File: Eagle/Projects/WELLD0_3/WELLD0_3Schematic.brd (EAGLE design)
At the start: 160 x 100 mm, 17 parts, among them J2 Battery, U1 EFM8BB10F8G-µCBRZ, U2 CJT1117-3.3-SOT223, X1 ProgramPins

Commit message: Circuit done - i guess 24/10-18
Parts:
- removed R1: 10K, audio amplifier example:R0603
- removed S1: Switch, SparkFun-Switches:TACTILE_SWITCH_SMD_6.2MM_TALL
- removed T1: (no value), DC_LOAD_AU:SOT23-BEC
- removed U1: EFM8BB10F8G-µCBRZ, adg451_adg452_adg453:SO16
- added ALT_USER_SW1, ALT_USER_SW2, ALT_USER_SW3, ALT_USER_SW4, LED+, LED-: (no value), SparkFun-Connectors:1X01
- added BOOTLOADER, RST_SW, USER_SW, USER_SW_ALT: Switch, SparkFun-Switches:TACTILE_SWITCH_SMD_6.2MM_TALL
- added C1, C2: 100nF, rcl:C0603
- added IC1: STM32F030F4P6TR, SamacSys_Parts:SOP65P640X120-20N
- added R2, R4: 10k, audio amplifier example:R0603
- added R3, R6: 10K, audio amplifier example:R0603
- added R5: R>12.5k, audio amplifier example:R0603
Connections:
- removed net C2D: U1.7, X1.3
- removed net P0.6: U1.13
- removed net P0.7: U1.12
- removed net RSTB/C2CI: U1.6, X1.2
- removed net SWSIGN: R1.1, S1.A2, U1.14
- removed net VDD: R1.2, U1.5, U2.2, U2.TER
- new net +3.3V: BOOTLOADER.A2, IC1.16, IC1.5, R3.2, R6.2, U2.2, U2.TER
- new net ADC_BATTERY: IC1.6, R4.2, R5.1
- new net N$4: ALT_USER_SW3.1, USER_SW_ALT.A2
- new net N$5: ALT_USER_SW4.1, USER_SW_ALT.B2
- new net N$6: IC1.1, R2.1
- new net NRST: C1.1, IC1.4, R6.1, RST_SW.B2
- new net SWSIGN1: ALT_USER_SW1.1, C2.1, IC1.13, R3.1, USER_SW.A2
- new net UART_RX: IC1.18, X1.2
- new net UART_TX: IC1.17, X1.3
- net +7.4V: now also R5.2
- net DIM: now also IC1.12; no longer U1.10
- net FB: now also LED-.1
- net GND: now also ALT_USER_SW2.1, BOOTLOADER.B2, C1.2, C2.2, IC1.15, R2.2, R4.1, RST_SW.A2, USER_SW.B2; no longer S1.B2, U1.4
- net INH: now also IC1.11
- net N$1: now also LED+.1

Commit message: Ready for final thoughts
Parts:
- removed X1: ProgramPins, con-molex:70543-03
- added PROGRAMPINS: (no value), con-lstb:MA04-1
- moved USER_SW_ALT 241.5 mm to (49.5, 40.6), turned to 270 degrees
- moved ALT_USER_SW4 232.3 mm to (55.9, 36.8)
- moved ALT_USER_SW3 223.6 mm to (43.2, 36.8)
- moved ALT_USER_SW2 211.9 mm to (61.0, 21.6)
- moved ALT_USER_SW1 202.8 mm to (61.0, 17.8)
- moved LED- 198.3 mm to (39.4, 27.9)
- moved LED+ 191.7 mm to (24.1, 27.9)
- moved R2 185.2 mm to (54.6, 16.5), turned to 90 degrees
- moved C2 179.5 mm to (59.7, 2.54)
- moved C1 176.9 mm to (45.7, 17.8)
- moved RST_SW 172.6 mm to (43.2, 22.9), turned to 180 degrees
- moved R6 161.4 mm to (41.9, 17.8)
- moved BOOTLOADER 157.4 mm to (53.3, 22.9), turned to 180 degrees
- moved R5 138.3 mm to (12.7, 25.4), turned to 90 degrees
- moved R4 133.3 mm to (16.5, 25.4), turned to 270 degrees
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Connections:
- net +7.4V: now also PROGRAMPINS.4
- net GND: now also PROGRAMPINS.3; no longer X1.1
- net SWSIGN1: now also IC1.8; no longer IC1.13
- net UART_RX: now also PROGRAMPINS.1; no longer X1.2
- net UART_TX: now also PROGRAMPINS.2; no longer X1.3
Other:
- board size 160 x 100 mm -> 63.5 x 47 mm

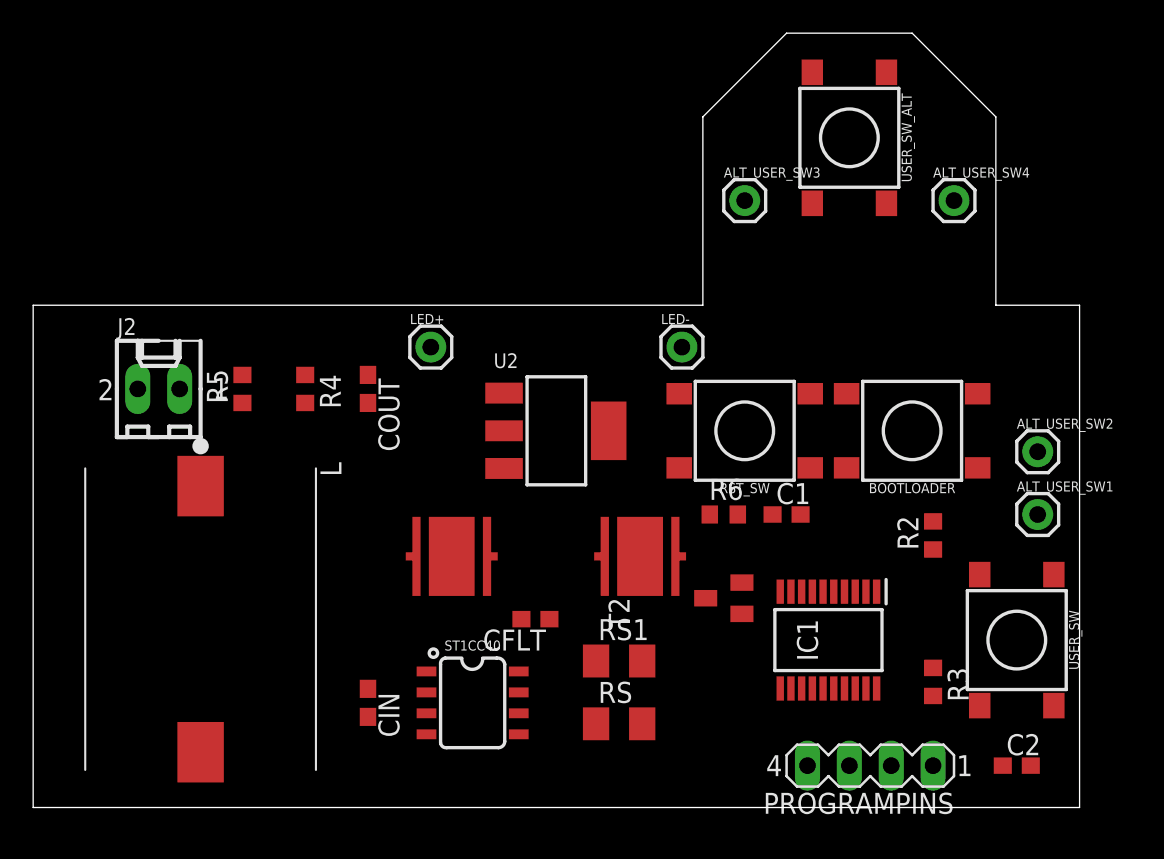
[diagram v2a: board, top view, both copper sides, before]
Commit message: Final form - missing heatsink
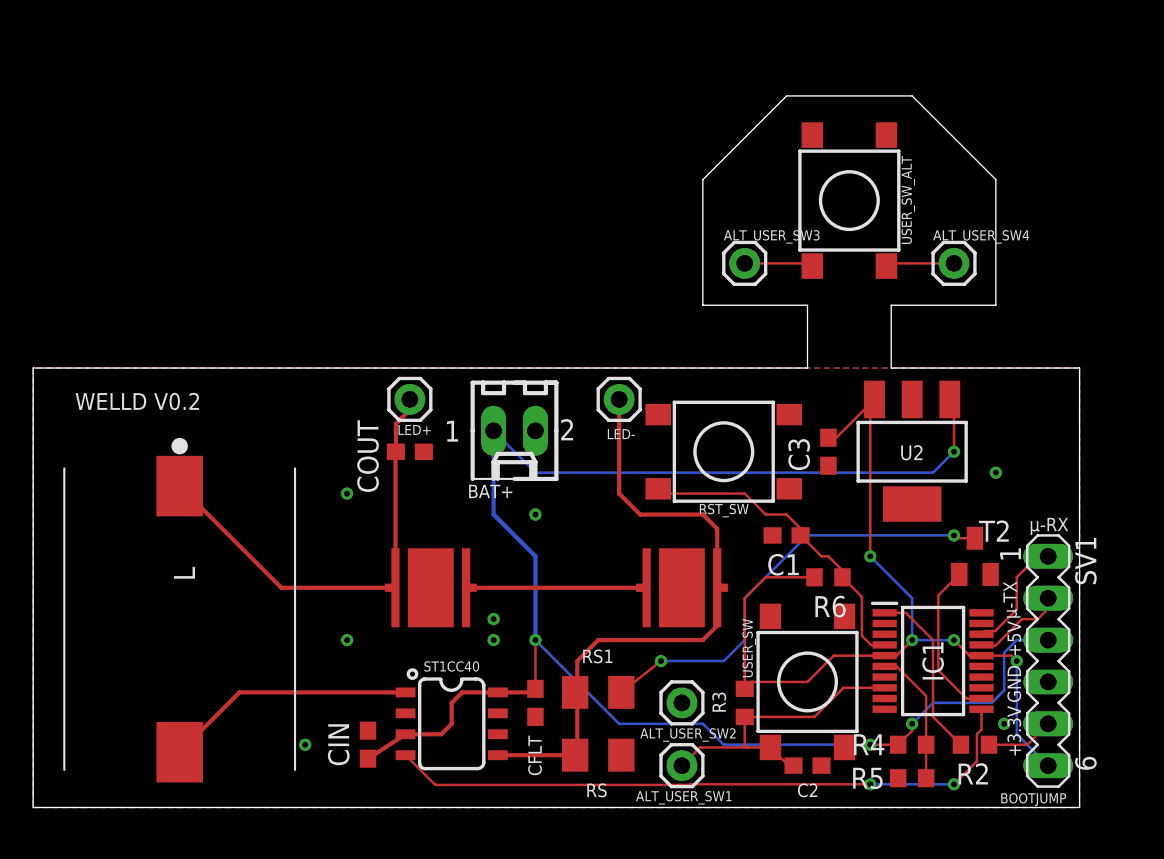
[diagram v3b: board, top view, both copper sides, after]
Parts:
- removed BOOTLOADER: Switch, SparkFun-Switches:TACTILE_SWITCH_SMD_6.2MM_TALL
- removed J2: Battery, con-molex:6410-02
- removed PROGRAMPINS: (no value), con-lstb:MA04-1
- added BAT+: BAT-, con-molex:6410-02
- added C3: 2.2µF, rcl:C0603
- added SV1: (no value), con-lstb:MA06-1
- moved R5 46.0 mm to (53.3, 3.81), turned to 180 degrees
- moved R4 43.8 mm to (53.3, 1.78), turned to 0 degrees
- moved ALT_USER_SW1 26.4 mm to (39.4, 2.54)
- moved ALT_USER_SW2 26.4 mm to (39.4, 6.35)
- moved U2 21.6 mm to (53.3, 21.6), turned to 180 degrees
- moved T2 15.5 mm to (57.1, 15.2), turned to 0 degrees
- moved R2 13.0 mm to (57.1, 3.81), turned to 0 degrees
- moved USER_SW 13.0 mm to (47.0, 7.62)
- moved C2 12.7 mm to (47.0, 2.54)
- moved R3 11.5 mm to (43.2, 6.35), turned to 90 degrees
- moved R6 7.41 mm to (48.3, 14.0), turned to 180 degrees
- moved IC1 6.48 mm to (54.6, 8.89), turned to 0 degrees
- moved CFLT 5.08 mm to (30.5, 6.35), turned to 90 degrees
- moved LED- 4.96 mm to (35.6, 24.8)
- moved COUT 4.58 mm to (22.9, 21.6), turned to 180 degrees
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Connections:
- new net BOOTJUMP: R2.2, SV1.5
- net +3.3V: now also C3.1, SV1.6, U2.3; no longer BOOTLOADER.A2, U2.2, U2.TER
- net +7.4V: now also BAT+.1, SV1.3, U2.1; no longer J2.1, PROGRAMPINS.4, U2.3
- net GND: now also BAT+.2, C3.2, SV1.4, U2.2, U2.TER; no longer BOOTLOADER.B2, J2.2, PROGRAMPINS.3, R2.2, U2.1
- net UART_RX: now also SV1.1; no longer PROGRAMPINS.1
- net UART_TX: now also SV1.2; no longer PROGRAMPINS.2
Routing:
- net +7.4V: track 0.00 -> 99.2 mm, vias 0 -> 4
- net +3.3V: track 0.00 -> 55.2 mm, vias 0 -> 4
- net FB: track 0.00 -> 39.4 mm
- net INH: track 0.00 -> 39.3 mm, vias 0 -> 2
- net N$3: track 0.00 -> 26.8 mm, vias 0 -> 2
- net N$1: track 0.00 -> 26.4 mm
- net NRST: track 0.00 -> 19.5 mm
- net SWSIGN1: track 0.00 -> 18.8 mm
- net SW: track 0.00 -> 15.2 mm
- net N$2: track 0.00 -> 11.0 mm
- net N$6: track 0.00 -> 10.7 mm
- net DIM: track 0.00 -> 9.68 mm
- net ADC_BATTERY: track 0.00 -> 7.63 mm
- net UART_RX: track 0.00 -> 7.15 mm
- net UART_TX: track 0.00 -> 5.64 mm
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- added copper zone on layer 1, net GND
- added copper zone on layer 16, net GND
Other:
- board size 63.5 x 47 mm -> 63.5 x 43.2 mm
- board text added: "+3.3V"
- board text added: "+5V"
- board text added: "BOOTJUMP"
- board text added: "GND"
- board text added: "WELLD V0.2"
- board text added: "µ-RX"
- board text added: "µ-TX"

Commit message: Ordered PCB
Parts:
- removed LED1, LED3: CREE-XLAMP-XM-L2, led:CREE-XLAMP-XM-L
- added LED2, LED4: CREE-XLAMP-XM-L, led1:CREE-XLAMP-XM-L
- moved U2 0.25 mm to (53.3, 21.3)
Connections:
- net FB: now also LED2.C, LED2.C@1; no longer LED3.C, LED3.C@1
- net GND: now also LED2.EXP, LED4.EXP
- net N$1: now also LED4.A, LED4.A@1; no longer LED1.A, LED1.A@1
- net N$2: now also LED2.A, LED2.A@1, LED4.C, LED4.C@1; no longer LED1.C, LED1.C@1, LED3.A, LED3.A@1
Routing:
- net GND: track 0.30 -> 27.3 mm, vias 8 -> 21
- net N$2: track 11.0 -> 12.7 mm
- net ADC_BATTERY: track 7.63 -> 8.31 mm
- net FB: track 39.4 -> 38.7 mm
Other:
- board text added: "V0.2"
- board text removed: "WELLD V0.2"
